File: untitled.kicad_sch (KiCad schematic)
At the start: 0 parts

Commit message: creating the file
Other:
- added sheet min (min.kicad_sch)
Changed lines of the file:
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@@
+		)
+	)
+	(sheet
+		(at 63.5 76.2)
+		(size 12.7 12.7)
+		(exclude_from_sim no)
+		(in_bom yes)
+		(on_board yes)
+		(dnp no)
+		(fields_autoplaced yes)
+		(stroke
+			(width 0.1524)
+			(type solid)
+		)
+		(fill
+			(color 0 0 0 0)
+		)
+		(property "Sheetname" "min"
+			(at 63.5 75.4884 0)
+			(show_name no)
+			(do_not_autoplace no)
+			(effects
+				(font
+					(size 1.27 1.27)
+				)
+				(justify left bottom)
+			)
+		)
+		(property "Sheetfile" "min.kicad_sch"
+			(at 63.5 89.4846 0)
+			(show_name no)
+			(do_not_autoplace no)
+			(effects
+				(font
+					(size 1.27 1.27)
+				)
+				(justify left top)
+			)
+		)
+		(instances
+			(project "BinaryClock"
+				(path "/b8db7867-2c41-4996-89b7-85623a375f4b/d72dbc43-5f9c-4389-b46b-bcc9f20f0691"
+					(page "5")
+				)
+			)
 		)
 	)

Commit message: finishing the min circuit nad conect it to its place
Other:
- sheet min ports: added CLK, h_clk, min-o_1, min-o_2, min-o_3, min-o_4, min-t_1, min-t_2, min-t_3, min-t_4; removed none
- sheet sec ports: added CLK, min_clk, sec-o_1, sec-o_2, sec-o_3, sec-o_4, sec-t_1, sec-t_2, sec-t_3, sec-t_4; removed none
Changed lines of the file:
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@@
 	(generator_version "10.0")
 	(paper "A4")
+	(wire
+		(pts
+			(xy 54.61 92.71) (xy 63.5 92.71)
+		)
+		(stroke
+			(width 0)
+			(type default)
+		)
+	)
+	(wire
+		(pts
+			(xy 33.02 92.71) (xy 38.1 92.71)
+		)
+		(stroke
+			(width 0)
+			(type default)
+		)
+	)
+	(hierarchical_label "CLK"
+		(shape input)
+		(at 33.02 92.71 180)
+		(effects
+			(font
+				(size 1.27 1.27)
+			)
+			(justify right)
+		)
+	)
 	(sheet
 		(at 38.1 76.2)
-		(size 12.7 12.7)
+		(size 16.51 31.75)
 		(exclude_from_sim no)
 		(in_bom yes)
@@
 		)
 		(property "Sheetfile" "sec.kicad_sch"
-			(at 38.1 89.4846 0)
+			(at 38.1 108.5346 0)
 			(show_name no)
 			(do_not_autoplace no)
@@
 				)
 				(justify left top)
+			)
+		)
+		(pin "sec-o_1" output
+			(at 40.64 107.95 270)
+			(effects
+				(font
+					(size 1.27 1.27)
+				)
+				(justify left)
+			)
+		)
+		(pin "sec-o_4" output
+			(at 52.07 107.95 270)
+			(effects
+				(font
+					(size 1.27 1.27)
+				)
+				(justify left)
+			)
+		)
+		(pin "sec-o_2" output
+			(at 44.45 107.95 270)
+			(effects
+				(font
+					(size 1.27 1.27)
+				)
+				(justify left)
+			)
+		)
+		(pin "CLK" output
+			(at 38.1 92.71 180)
+			(effects
+				(font
+					(size 1.27 1.27)
+				)
+				(justify left)
+			)
+		)
+		(pin "sec-t_1" output
+			(at 40.64 76.2 90)
+			(effects
+				(font
+					(size 1.27 1.27)
+				)
+				(justify right)
+			)
+		)
+		(pin "sec-t_3" output
+			(at 48.26 76.2 90)
+			(effects
+				(font
+					(size 1.27 1.27)
+				)
+				(justify right)
+			)
+		)
+		(pin "sec-t_2" output
+			(at 44.45 76.2 90)
+			(effects
+				(font
+					(size 1.27 1.27)
+				)
+				(justify right)
+			)
+		)
+		(pin "sec-t_4" output
+			(at 52.07 76.2 90)
+			(effects
+				(font
+					(size 1.27 1.27)
+				)
+				(justify right)
+			)
+		)
+		(pin "min_clk" output
+			(at 54.61 92.71 0)
+			(effects
+				(font
+					(size 1.27 1.27)
+				)
+				(justify right)
+			)
+		)
+		(pin "sec-o_3" output
+			(at 48.26 107.95 270)
+			(effects
+				(font
+					(size 1.27 1.27)
+				)
+				(justify left)
 			)
 		)
@@
 	(sheet
 		(at 63.5 76.2)
-		(size 12.7 12.7)
+		(size 16.51 31.75)
 		(exclude_from_sim no)
 		(in_bom yes)
@@
 		)
 		(property "Sheetfile" "min.kicad_sch"
-			(at 63.5 89.4846 0)
+			(at 63.5 108.5346 0)
 			(show_name no)
 			(do_not_autoplace no)
@@
 			)
 		)
+		(pin "min-o_3" output
+			(at 73.66 107.95 270)
+			(effects
+				(font
+					(size 1.27 1.27)
+				)
+				(justify left)
+			)
+		)
+		(pin "min-t_3" output
+			(at 73.66 76.2 90)
+			(effects
+				(font
+					(size 1.27 1.27)
+				)
+				(justify right)
+			)
+		)
+		(pin "min-o_4" output
+			(at 77.47 107.95 270)
+			(effects
+				(font
+					(size 1.27 1.27)
+				)
+				(justify left)
+			)
+		)
+		(pin "min-t_1" output
+			(at 66.04 76.2 90)
+			(effects
+				(font
+					(size 1.27 1.27)
+				)
+				(justify right)
+			)
+		)
+		(pin "min-o_1" output
+			(at 66.04 107.95 270)
+			(effects
+				(font
+					(size 1.27 1.27)
+				)
+				(justify left)
+			)
+		)
+		(pin "min-o_2" output
+			(at 69.85 107.95 270)
+			(effects
+				(font
+					(size 1.27 1.27)
+				)
+				(justify left)
+			)
+		)
+		(pin "min-t_2" output
+			(at 69.85 76.2 90)
+			(effects
+				(font
+					(size 1.27 1.27)
+				)
+				(justify right)
+			)
+		)
+		(pin "h_clk" output
+			(at 80.01 92.71 0)
+			(effects
+				(font
+					(size 1.27 1.27)
+				)
+				(justify right)
+			)
+		)
+		(pin "min-t_4" output
+			(at 77.47 76.2 90)
+			(effects
+				(font
+					(size 1.27 1.27)
+				)
+				(justify right)
+			)
+		)
+		(pin "CLK" output
+			(at 63.5 92.71 180)
+			(effects
+				(font
+					(size 1.27 1.27)
+				)
+				(justify left)
+			)
+		)

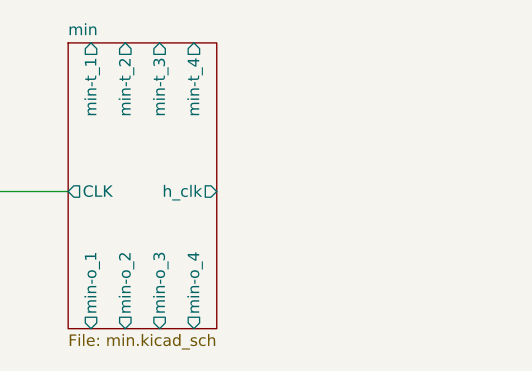
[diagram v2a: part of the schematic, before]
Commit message: creating the file and copiing the template
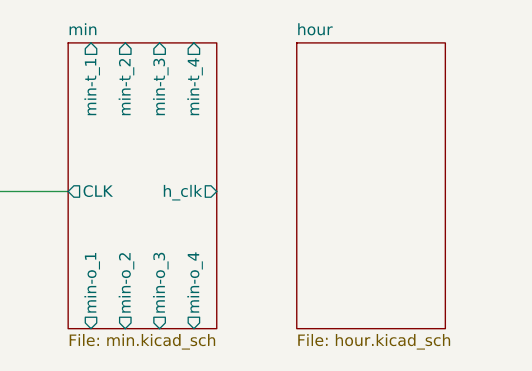
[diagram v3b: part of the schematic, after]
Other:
- added sheet hour (hour.kicad_sch)
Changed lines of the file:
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@@
+		)
+	)
+	(sheet
+		(at 88.9 76.2)
+		(size 16.51 31.75)
+		(exclude_from_sim no)
+		(in_bom yes)
+		(on_board yes)
+		(dnp no)
+		(fields_autoplaced yes)
+		(stroke
+			(width 0.1524)
+			(type solid)
+		)
+		(fill
+			(color 0 0 0 0)
+		)
+		(property "Sheetname" "hour"
+			(at 88.9 75.4884 0)
+			(show_name no)
+			(do_not_autoplace no)
+			(effects
+				(font
+					(size 1.27 1.27)
+				)
+				(justify left bottom)
+			)
+		)
+		(property "Sheetfile" "hour.kicad_sch"
+			(at 88.9 108.5346 0)
+			(show_name no)
+			(do_not_autoplace no)
+			(effects
+				(font
+					(size 1.27 1.27)
+				)
+				(justify left top)
+			)
+		)
+		(instances
+			(project "BinaryClock"
+				(path "/b8db7867-2c41-4996-89b7-85623a375f4b/d72dbc43-5f9c-4389-b46b-bcc9f20f0691"
+					(page "6")
+				)
+			)
 		)
 	)

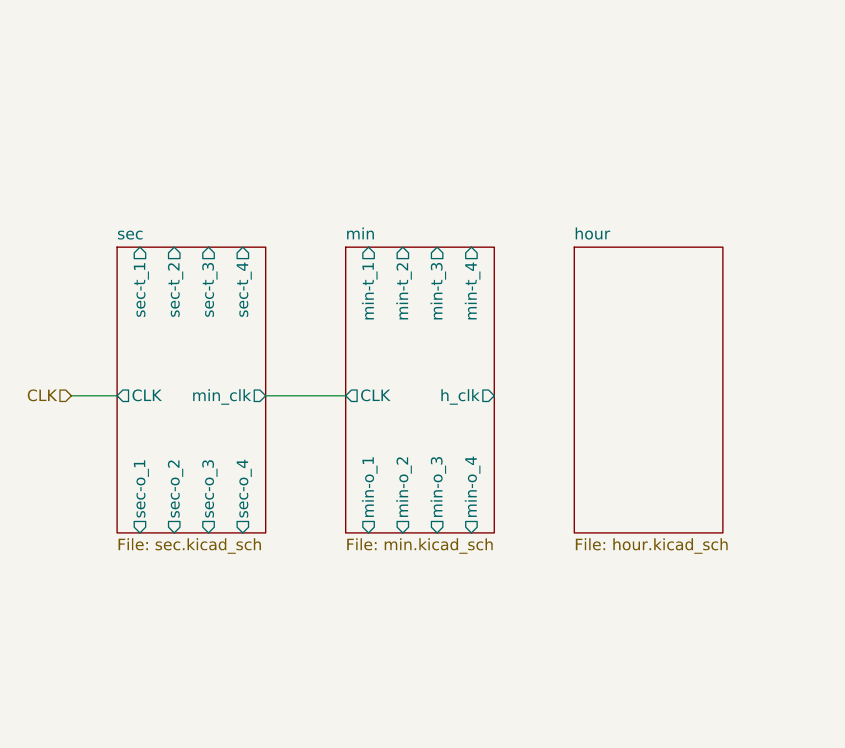
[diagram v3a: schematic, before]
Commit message: Making the 24 rst for ewery counter and adding Capacitors
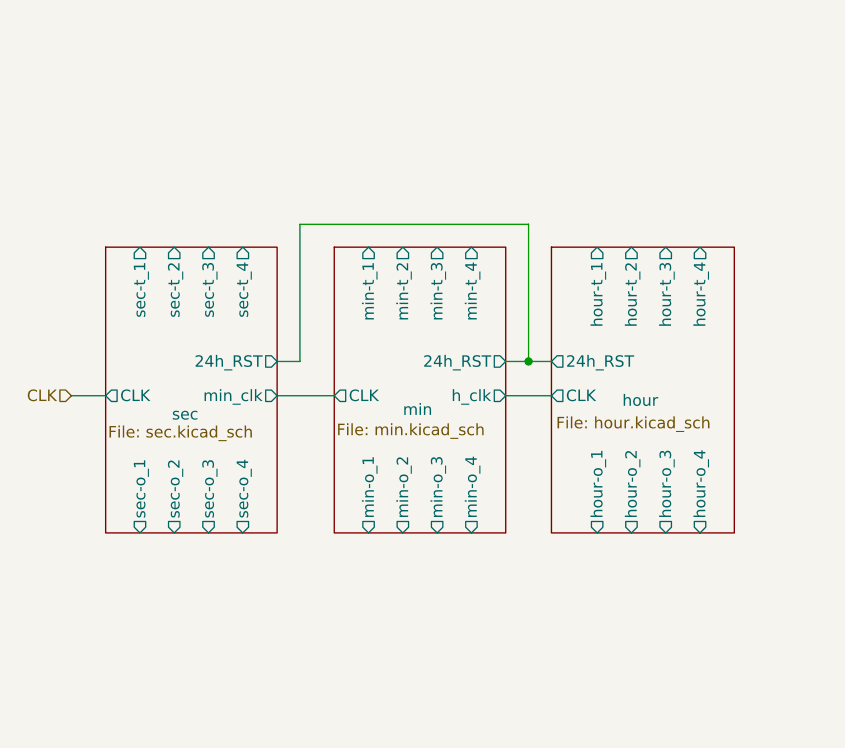
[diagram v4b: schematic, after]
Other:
- sheet hour ports: added 24h_RST, CLK, hour-o_1, hour-o_2, hour-o_3, hour-o_4, hour-t_1, hour-t_2, hour-t_3, hour-t_4; removed none
- sheet min ports: added 24h_RST; removed none
- sheet sec ports: added 24h_RST; removed none
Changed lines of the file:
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@@
 	(generator_version "10.0")
 	(paper "A4")
-	(wire
-		(pts
-			(xy 54.61 92.71) (xy 63.5 92.71)
-		)
-		(stroke
-			(width 0)
-			(type default)
-		)
-	)
-	(wire
-		(pts
-			(xy 33.02 92.71) (xy 38.1 92.71)
+	(junction
+		(at 83.82 88.9)
+		(diameter 0)
+		(color 0 0 0 0)
+	)
+	(wire
+		(pts
+			(xy 55.88 92.71) (xy 62.23 92.71)
+		)
+		(stroke
+			(width 0)
+			(type default)
+		)
+	)
+	(wire
+		(pts
+			(xy 33.02 92.71) (xy 36.83 92.71)
+		)
+		(stroke
+			(width 0)
+			(type default)
+		)
+	)
+	(wire
+		(pts
+			(xy 55.88 88.9) (xy 58.42 88.9)
+		)
+		(stroke
+			(width 0)
+			(type default)
+		)
+	)
+	(wire
+		(pts
+			(xy 58.42 73.66) (xy 83.82 73.66)
+		)
+		(stroke
+			(width 0)
+			(type default)
+		)
+	)
+	(wire
+		(pts
+			(xy 58.42 88.9) (xy 58.42 73.66)
+		)
+		(stroke
+			(width 0)
+			(type default)
+		)
+	)
+	(wire
+		(pts
+			(xy 81.28 88.9) (xy 83.82 88.9)
+		)
+		(stroke
+			(width 0)
+			(type default)
+		)
+	)
+	(wire
+		(pts
+			(xy 83.82 88.9) (xy 86.36 88.9)
+		)
+		(stroke
+			(width 0)
+			(type default)
+		)
+	)
+	(wire
+		(pts
+			(xy 83.82 73.66) (xy 83.82 88.9)
+		)
+		(stroke
+			(width 0)
+			(type default)
+		)
+	)
+	(wire
+		(pts
+			(xy 81.28 92.71) (xy 86.36 92.71)
 		)
 		(stroke
@@
 	)
 	(sheet
-		(at 38.1 76.2)
-		(size 16.51 31.75)
+		(at 36.83 76.2)
+		(size 19.05 31.75)
 		(exclude_from_sim no)
 		(in_bom yes)
 		(on_board yes)
 		(dnp no)
-		(fields_autoplaced yes)
 		(stroke
 			(width 0.1524)
@@
 		)
 		(property "Sheetname" "sec"
-			(at 38.1 75.4884 0)
+			(at 44.196 95.504 0)
 			(show_name no)
 			(do_not_autoplace no)
@@
 		)
 		(property "Sheetfile" "sec.kicad_sch"
-			(at 38.1 108.5346 0)
+			(at 37.084 96.012 0)
 			(show_name no)
 			(do_not_autoplace no)
@@
 		)
 		(pin "CLK" output
-			(at 38.1 92.71 180)
+			(at 36.83 92.71 180)
 			(effects
 				(font
@@
 		)
 		(pin "min_clk" output
-			(at 54.61 92.71 0)
+			(at 55.88 92.71 0)
 			(effects
 				(font
@@
 				)
 				(justify left)
+			)
+		)
+		(pin "24h_RST" output
+			(at 55.88 88.9 0)
+			(effects
+				(font
+					(size 1.27 1.27)
+				)
+				(justify right)
 			)
 		)
@@
 	)
 	(sheet
-		(at 63.5 76.2)
-		(size 16.51 31.75)
+		(at 62.23 76.2)
+		(size 19.05 31.75)
 		(exclude_from_sim no)
 		(in_bom yes)
 		(on_board yes)
 		(dnp no)
-		(fields_autoplaced yes)
 		(stroke
 			(width 0.1524)
@@
 		)
 		(property "Sheetname" "min"
-			(at 63.5 75.4884 0)
+			(at 69.85 94.996 0)
 			(show_name no)
 			(do_not_autoplace no)
@@
 		)
 		(property "Sheetfile" "min.kicad_sch"
-			(at 63.5 108.5346 0)
+			(at 62.484 95.758 0)
 			(show_name no)
 			(do_not_autoplace no)
@@
 		)
 		(pin "h_clk" output
-			(at 80.01 92.71 0)
+			(at 81.28 92.71 0)
 			(effects
 				(font
@@
 		)
 		(pin "CLK" output
-			(at 63.5 92.71 180)
-			(effects
-				(font
-					(size 1.27 1.27)
-				)
-				(justify left)
+			(at 62.23 92.71 180)
+			(effects
+				(font
+					(size 1.27 1.27)
+				)
+				(justify left)
+			)
+		)
+		(pin "24h_RST" output
+			(at 81.28 88.9 0)
+			(effects
+				(font
+					(size 1.27 1.27)
+				)
+				(justify right)
 			)
 		)
@@
 	)
 	(sheet
-		(at 88.9 76.2)
-		(size 16.51 31.75)
+		(at 86.36 76.2)
+		(size 20.32 31.75)
 		(exclude_from_sim no)
 		(in_bom yes)
 		(on_board yes)
 		(dnp no)
-		(fields_autoplaced yes)
 		(stroke
 			(width 0.1524)
@@
 		)
 		(property "Sheetname" "hour"
-			(at 88.9 75.4884 0)
+			(at 94.234 93.98 0)
 			(show_name no)
 			(do_not_autoplace no)
@@
 		)
 		(property "Sheetfile" "hour.kicad_sch"
-			(at 88.9 108.5346 0)
+			(at 86.868 94.996 0)
 			(show_name no)
 			(do_not_autoplace no)
@@
 			)
 		)
+		(pin "24h_RST" output
+			(at 86.36 88.9 180)
+			(effects
+				(font
+					(size 1.27 1.27)
+				)
+				(justify left)
+			)
+		)
+		(pin "CLK" output
+			(at 86.36 92.71 180)
+			(effects
+				(font
+					(size 1.27 1.27)
+				)
+				(justify left)
+			)
+		)
+		(pin "hour-o_1" output
+			(at 91.44 107.95 270)
+			(effects
+				(font
+					(size 1.27 1.27)
+				)
+				(justify left)
+			)
+		)
+		(pin "hour-o_2" output
+			(at 95.25 107.95 270)
+			(effects
+				(font
+					(size 1.27 1.27)
+				)
+				(justify left)
+			)
+		)
+		(pin "hour-o_3" output
+			(at 99.06 107.95 270)
+			(effects
+				(font
+					(size 1.27 1.27)
+				)
+				(justify left)
+			)
+		)
+		(pin "hour-o_4" output
+			(at 102.87 107.95 270)
+			(effects
+				(font
+					(size 1.27 1.27)
+				)
+				(justify left)
+			)
+		)
+		(pin "hour-t_1" output
+			(at 91.44 76.2 90)
+			(effects
+				(font
+					(size 1.27 1.27)
+				)
+				(justify right)
+			)
+		)
+		(pin "hour-t_2" output
+			(at 95.25 76.2 90)
+			(effects
+				(font
+					(size 1.27 1.27)
+				)
+				(justify right)
+			)
+		)
+		(pin "hour-t_3" output
+			(at 99.06 76.2 90)
+			(effects
+				(font
+					(size 1.27 1.27)
+				)
+				(justify right)
+			)
+		)
+		(pin "hour-t_4" output
+			(at 102.87 76.2 90)
+			(effects
+				(font
+					(size 1.27 1.27)
+				)
+				(justify right)
+			)
+		)

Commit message: Cleaning the shematic
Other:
- added sheet hour_display (sec_display.kicad_sch)
- added sheet min_display (sec_display.kicad_sch)
- added sheet sec_display (sec_display.kicad_sch)
- added sheet t-hour_display (sec_display.kicad_sch)
- added sheet t-min_display (sec_display.kicad_sch)
- added sheet t-sec_display (sec_display.kicad_sch)
